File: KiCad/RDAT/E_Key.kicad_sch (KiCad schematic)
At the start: 0 parts

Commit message: Connected m.2 E Key
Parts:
- added C80, C81: 220nF/50V, A_HDJ_Library:C_0402_1005Metric, symbol Device:C_Small
- added C82, C84: 10uF/10V, A_HDJ_Library:C_0402_1005Metric, symbol Device:C
- added C83, C85: 100nF/50V, A_HDJ_Library:C_0402_1005Metric, symbol Device:C
- added H8: MountingHole_M2.0, A_HDJ_Library:MountingHole_2.75mm_M2_4.4mm_Pad_TopOnly, symbol Mechanical:MountingHole_Pad
- added J16: Bus_M.2_Socket_E, A_HDJ_Library:PCIe_M.2_Connectors_P=0.5mm_H=4.2mm_KeyE, symbol Connector:Bus_M.2_Socket_E
- added R72, R73: 0R/1%, A_HDJ_Library:R_0402_1005Metric, symbol Device:R
- added R74, R75: 10K/1%, A_HDJ_Library:R_0402_1005Metric, symbol Device:R
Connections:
- new net: J16.56 (~{W_DISABLE1}), R74.1
- new net: J16.50 (SUSCLK), R73.1
- new net: J16.54 (~{W_DISABLE2}), R75.2
- new net +3V3: C82.2, C83.2, C84.2, C85.2, J16.2 (3.3V), J16.4 (3.3V), J16.72 (3.3V), J16.74 (3.3V), R74.2, R75.1
- new net CON_PCIE_TX_0+: C80.2, J16.35 (PETp0)
- new net CON_PCIE_TX_0-: C81.2, J16.37 (PETn0)
- new net GND: C82.1, C83.1, C84.1, C85.1, H8.1, J16.1 (GND), J16.18 (GND), J16.33 (GND), J16.39 (GND), J16.45 (GND), J16.51 (GND), J16.57 (GND), J16.63 (GND), J16.69 (GND), J16.7 (GND), J16.75 (GND), J16.MP1, J16.MP2, R72.2
- new net PCIE_RX_0+: J16.41 (PERp0)
- new net PCIE_RX_0-: J16.43 (PERn0)
- new net PCIE_TX_0+: C80.1
- new net PCIE_TX_0-: C81.1
- new net REFCLKE+: J16.47 (REFCLKp0)
- new net REFCLKE-: J16.49 (REFCLKn0)
- new net SUSCLK: R73.2
- new net USB_2_P7+: J16.3 (USB_D+)
- new net USB_2_P7-: J16.5 (USB_D-)
- new net ~{CLKREQE}: J16.53 (~{CLKREQ0}), R72.1
- new net ~{PLT_RST}: J16.52 (~{PERST0})
- new net ~{WAKE}: J16.55 (~{PEWAKE0})
- no-connect marks 0 -> 38

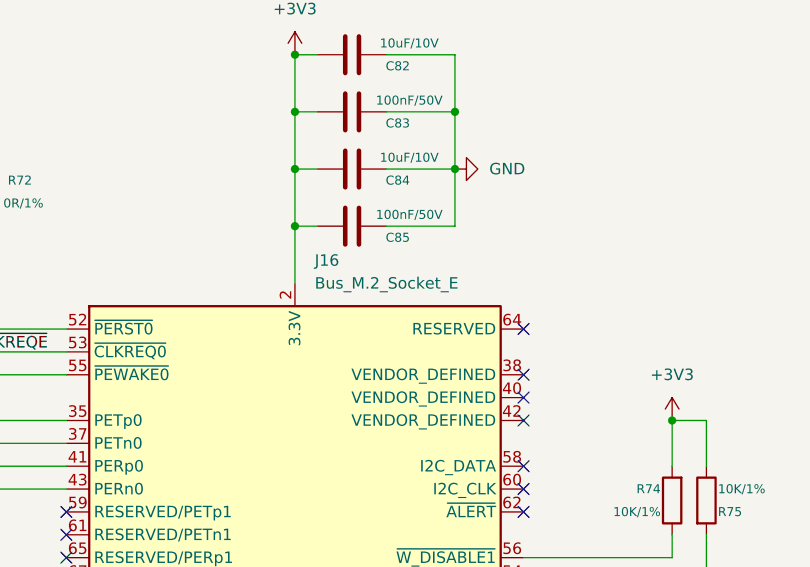
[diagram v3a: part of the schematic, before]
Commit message: Added Libs and DOCS
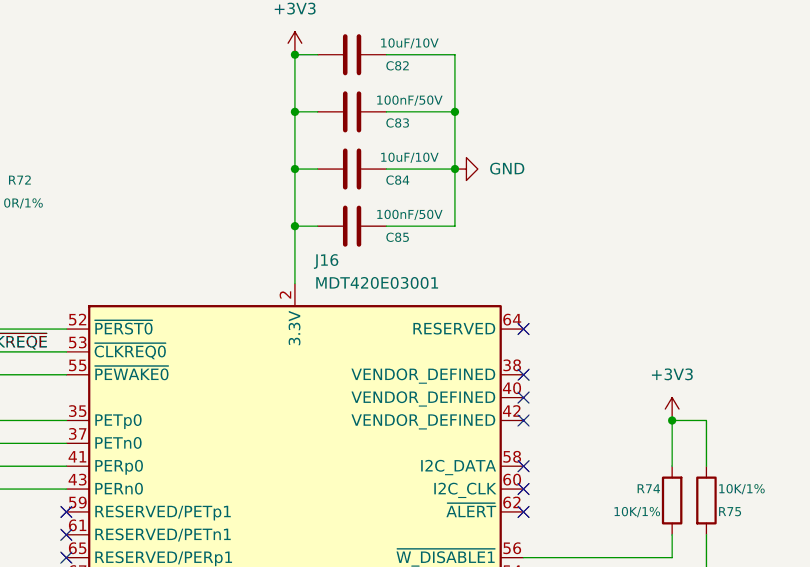
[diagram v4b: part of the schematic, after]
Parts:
- J16: value Bus_M.2_Socket_E -> MDT420E03001; footprint A_HDJ_Library:PCIe_M.2_Connectors_P=0.5mm_H=4.2mm_KeyE -> footprints:AMPHENOL_MDT420E03001; JLCPCB_LINK (none) -> https://jlcpcb.com/partdetail/AmphenolIcc-MDT420E03001/C599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
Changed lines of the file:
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@@
 			)
 		)
-		(property "Value" "Bus_M.2_Socket_E"
+		(property "Value" "MDT420E03001"
 			(at 139.3541 69.85 0)
 			(effects
@@
 			)
 		)
-		(property "Footprint" "A_HDJ_Library:PCIe_M.2_Connectors_P=0.5mm_H=4.2mm_KeyE"
+		(property "Footprint" "footprints:AMPHENOL_MDT420E03001"
 			(at 137.16 91.44 0)
 			(effects
@@
 			)
 		)
-		(property "Datasheet" "http://read.pudn.com/downloads794/doc/project/3133918/PCIe_M.2_Electromechanical_Spec_Rev1.0_Final_11012013_RS_Clean.pdf#page=150"
+		(property "Datasheet" "https://cdn.amphenol-cs.com/media/wysiwyg/files/documentation/datasheet/ssio/ssio_pcie_m2.pdf"
 			(at 137.16 91.44 0)
 			(effects
@@
 			)
 		)
-		(property "JLCPCB_LINK" ""
+		(property "JLCPCB_LINK" "https://jlcpcb.com/partdetail/AmphenolIcc-MDT420E03001/C599397"
 			(at 137.16 118.11 0)
 			(effects
@@
 					(size 1.27 1.27)
 				)
+				(hide yes)
 			)
 		)

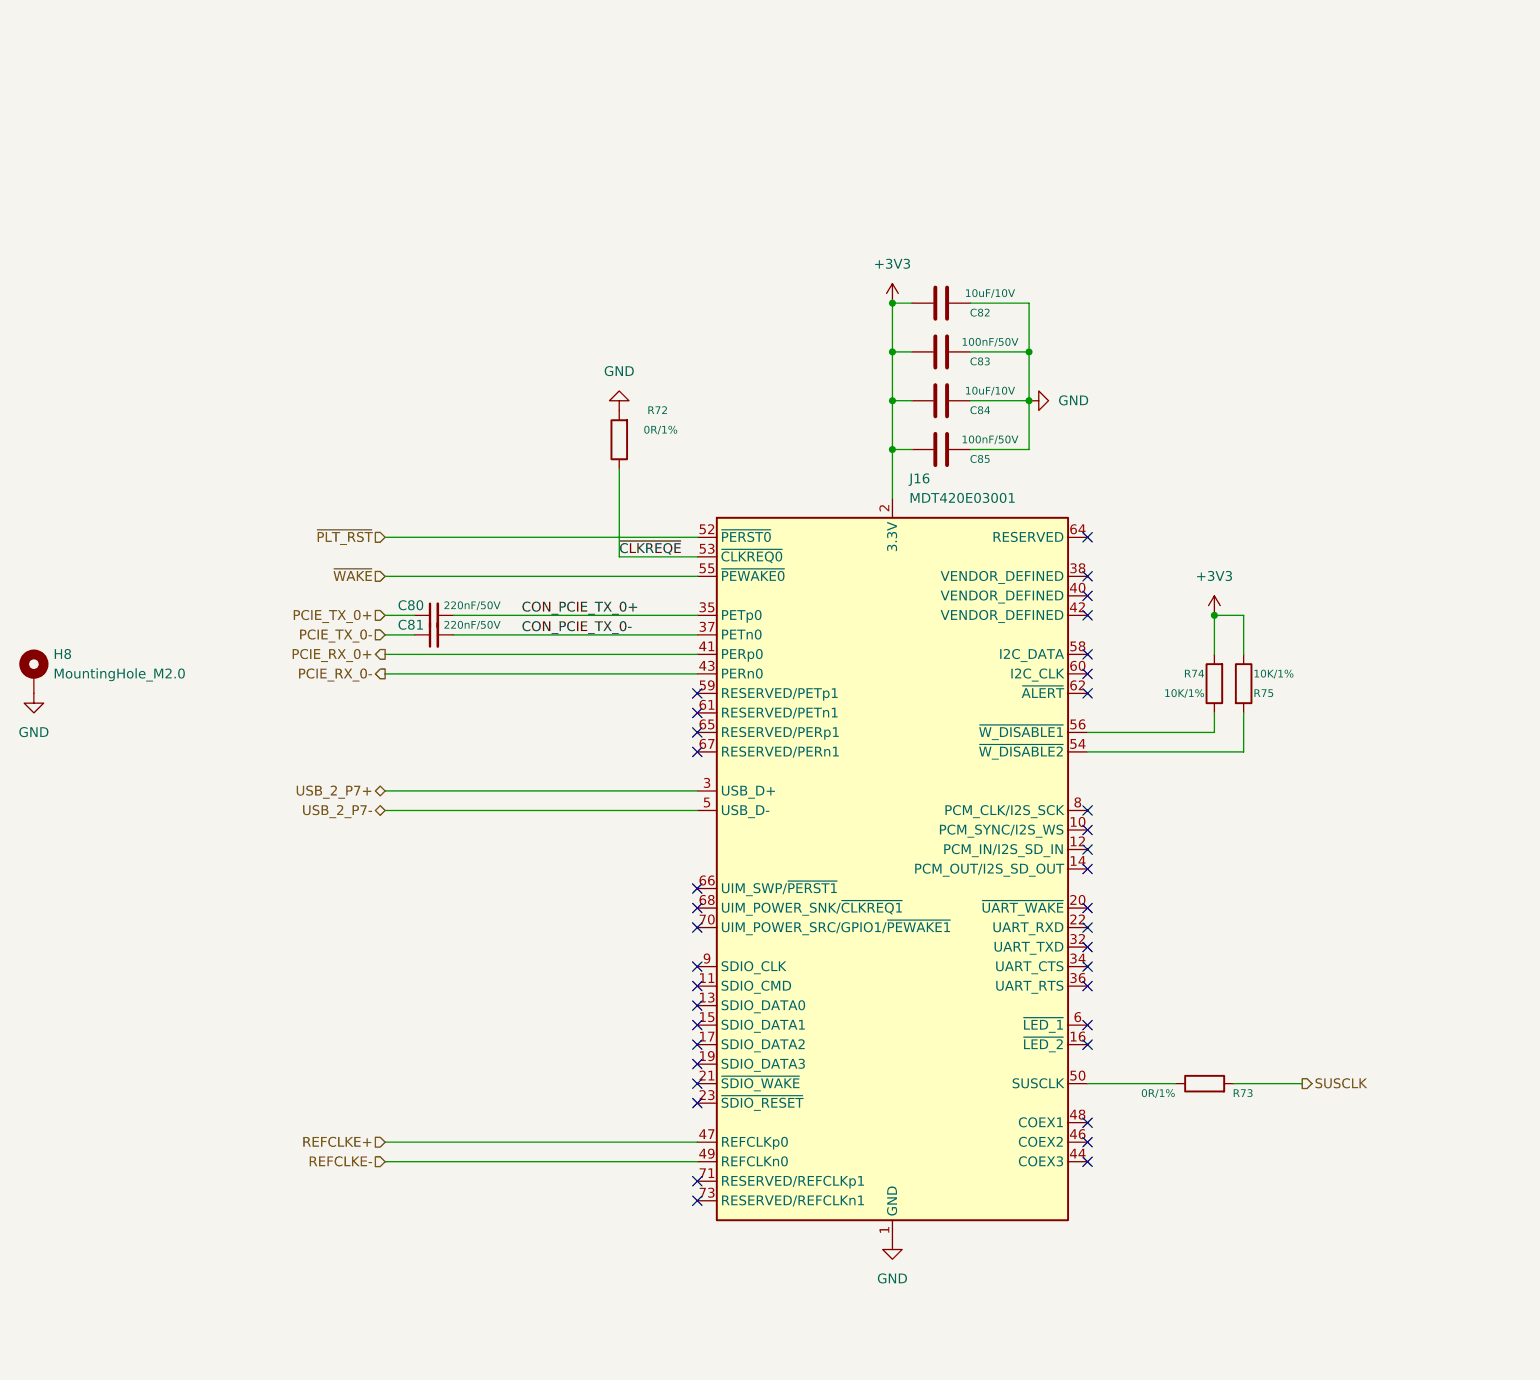
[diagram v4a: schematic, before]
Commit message: Sourced and documented all parts
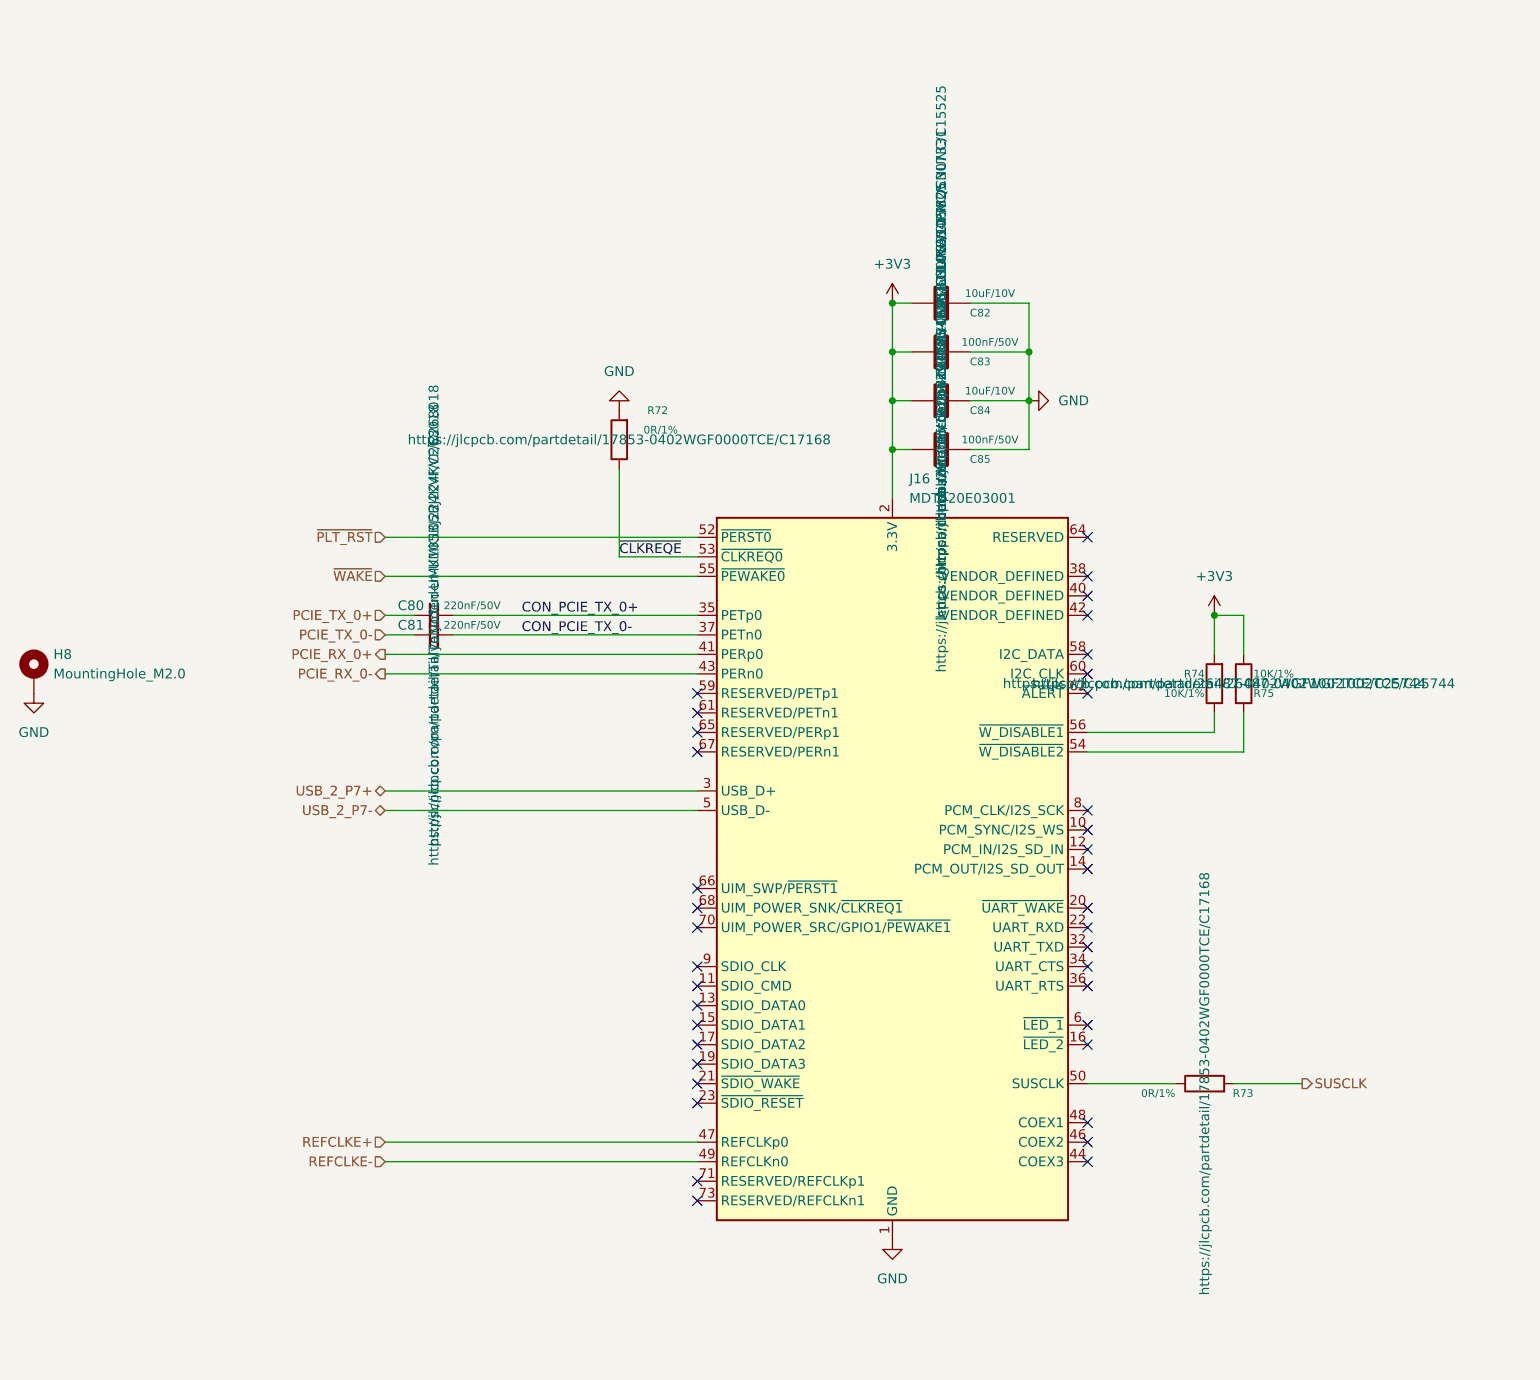
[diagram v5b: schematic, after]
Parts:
- C80, C81: JLCPCB_LINK (none) -> https://jlcpcb.com/partdetail/TaiyoYuden-UMK105BJ224KVF/C26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
- C82, C84: JLCPCB_LINK (none) -> https://jlcpcb.com/partdetail/16204-CL05A106MQ5NUNC/C15525
- C83, C85: JLCPCB_LINK (none) -> https://jlcpcb.com/partdetail/291005-CL05B104KB54PNC/C307331
- R72, R73: JLCPCB_LINK (none) -> https://jlcpcb.com/partdetail/17853-0402WGF0000TCE/C17168
- R74, R75: JLCPCB_LINK (none) -> https://jlcpcb.com/partdetail/26487-0402WGF1002TCE/C25744
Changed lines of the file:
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@@
 			)
 		)
-		(property "Datasheet" "~"
+		(property "Datasheet" "https://wmsc.lcsc.com/wmsc/upload/file/pdf/v2/lcsc/2108160930_Taiyo-Yuden-UMK105BJ224KV-F_C268018.pdf"
 			(at 77.47 85.09 0)
 			(effects
@@
 			)
 		)
-		(property "JLCPCB_LINK" ""
+		(property "JLCPCB_LINK" "https://jlcpcb.com/partdetail/TaiyoYuden-UMK105BJ224KVF/C268018"
 			(at 77.47 85.09 0)
 			(effects
@@
 			)
 		)
-		(property "Datasheet" "~"
+		(property "Datasheet" "https://wmsc.lcsc.com/wmsc/upload/file/pdf/v2/lcsc/2108160930_Taiyo-Yuden-UMK105BJ224KV-F_C268018.pdf"
 			(at 77.47 87.63 0)
 			(effects
@@
 			)
 		)
-		(property "JLCPCB_LINK" ""
+		(property "JLCPCB_LINK" "https://jlcpcb.com/partdetail/TaiyoYuden-UMK105BJ224KVF/C268018"
 			(at 77.47 87.63 0)
 			(effects
@@
 			)
 		)
-		(property "Datasheet" "~"
+		(property "Datasheet" "https://jlcpcb.com/api/file/downloadByFileSystemAccessId/8556212101498380288"
 			(at 179.07 93.98 0)
 			(effects
@@
 			)
 		)
-		(property "JLCPCB_LINK" ""
+		(property "JLCPCB_LINK" "https://jlcpcb.com/partdetail/26487-0402WGF1002TCE/C25744"
 			(at 179.07 93.98 0)
 			(effects
@@
 			)
 		)
-		(property "Datasheet" "~"
+		(property "Datasheet" "https://jlcpcb.com/api/file/downloadByFileSystemAccessId/8579707190011494400"
 			(at 143.51 57.15 0)
 			(effects
@@
 			)
 		)
-		(property "JLCPCB_LINK" ""
+		(property "JLCPCB_LINK" "https://jlcpcb.com/partdetail/16204-CL05A106MQ5NUNC/C15525"
 			(at 143.51 57.15 0)
 			(effects
@@
 			)
 		)
-		(property "Datasheet" "~"
+		(property "Datasheet" "https://jlcpcb.com/api/file/downloadByFileSystemAccessId/8579707190011494400"
 			(at 143.51 44.45 0)
 			(effects
@@
 			)
 		)
-		(property "JLCPCB_LINK" ""
+		(property "JLCPCB_LINK" "https://jlcpcb.com/partdetail/16204-CL05A106MQ5NUNC/C15525"
 			(at 143.51 44.45 0)
 			(effects
@@
 			)
 		)
-		(property "Datasheet" "~"
+		(property "Datasheet" "https://jlcpcb.com/api/file/downloadByFileSystemAccessId/8579705904671227904"
 			(at 177.8 146.05 0)
 			(effects
@@
 			)
 		)
-		(property "JLCPCB_LINK" ""
+		(property "JLCPCB_LINK" "https://jlcpcb.com/partdetail/17853-0402WGF0000TCE/C17168"
 			(at 177.8 146.05 0)
 			(effects
@@
 			)
 		)
-		(property "Datasheet" "~"
+		(property "Datasheet" "https://jlcpcb.com/api/file/downloadByFileSystemAccessId/8579705904671227904"
 			(at 101.6 62.23 0)
 			(effects
@@
 			)
 		)
-		(property "JLCPCB_LINK" ""
+		(property "JLCPCB_LINK" "https://jlcpcb.com/partdetail/17853-0402WGF0000TCE/C17168"
 			(at 101.6 62.23 0)
 			(effects
@@
 			)
 		)
-		(property "Datasheet" "~"
+		(property "Datasheet" "https://jlcpcb.com/api/file/downloadByFileSystemAccessId/8554627388281098240"
 			(at 143.51 63.5 0)
 			(effects
@@
 			)
 		)
-		(property "JLCPCB_LINK" ""
+		(property "JLCPCB_LINK" "https://jlcpcb.com/partdetail/291005-CL05B104KB54PNC/C307331"
 			(at 143.51 63.5 0)
 			(effects
@@
 			)
 		)
-		(property "Datasheet" "~"
+		(property "Datasheet" "https://jlcpcb.com/api/file/downloadByFileSystemAccessId/8554627388281098240"
 			(at 143.51 50.8 0)
 			(effects
@@
 			)
 		)
-		(property "JLCPCB_LINK" ""
+		(property "JLCPCB_LINK" "https://jlcpcb.com/partdetail/291005-CL05B104KB54PNC/C307331"
 			(at 143.51 50.8 0)
 			(effects
@@
 			)
 		)
-		(property "Datasheet" "~"
+		(property "Datasheet" "https://jlcpcb.com/api/file/downloadByFileSystemAccessId/8556212101498380288"
 			(at 182.88 93.98 0)
 			(effects
@@
 			)
 		)
-		(property "JLCPCB_LINK" ""
+		(property "JLCPCB_LINK" "https://jlcpcb.com/partdetail/26487-0402WGF1002TCE/C25744"
 			(at 182.88 93.98 0)
 			(effects

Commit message: Push before Board Layout
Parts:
- C80, C81, C82, C83, C84, C85: footprint A_HDJ_Library:C_0402_1005Metric -> Capacitor_SMD:C_0402_1005Metric
- H8: footprint A_HDJ_Library:MountingHole_2.75mm_M2_4.4mm_Pad_TopOnly -> MountingHole:MountingHole_2.2mm_M2_Pad_TopBottom
- R72, R73, R74, R75: footprint A_HDJ_Library:R_0402_1005Metric -> Resistor_SMD:R_0402_1005Metric
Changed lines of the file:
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@@
 			)
 		)
-		(property "Footprint" "A_HDJ_Library:C_0402_1005Metric"
+		(property "Footprint" "Capacitor_SMD:C_0402_1005Metric"
 			(at 77.47 85.09 0)
 			(effects
@@
 					(size 1.27 1.27)
 				)
+				(hide yes)
 			)
 		)
@@
 			)
 		)
-		(property "Footprint" "A_HDJ_Library:C_0402_1005Metric"
+		(property "Footprint" "Capacitor_SMD:C_0402_1005Metric"
 			(at 77.47 87.63 0)
 			(effects
@@
 					(size 1.27 1.27)
 				)
+				(hide yes)
 			)
 		)
@@
 			)
 		)
-		(property "Footprint" "A_HDJ_Library:R_0402_1005Metric"
+		(property "Footprint" "Resistor_SMD:R_0402_1005Metric"
 			(at 180.848 93.98 90)
 			(effects
@@
 			)
 		)
-		(property "Footprint" "A_HDJ_Library:C_0402_1005Metric"
+		(property "Footprint" "Capacitor_SMD:C_0402_1005Metric"
 			(at 139.7 58.1152 0)
 			(effects
@@
 					(size 1.27 1.27)
 				)
+				(hide yes)
 			)
 		)
@@
 			)
 		)
-		(property "Footprint" "A_HDJ_Library:C_0402_1005Metric"
+		(property "Footprint" "Capacitor_SMD:C_0402_1005Metric"
 			(at 139.7 45.4152 0)
 			(effects
@@
 					(size 1.27 1.27)
 				)
+				(hide yes)
 			)
 		)
@@
 			)
 		)
-		(property "Footprint" "A_HDJ_Library:R_0402_1005Metric"
+		(property "Footprint" "Resistor_SMD:R_0402_1005Metric"
 			(at 177.8 147.828 90)
 			(effects
@@
 			)
 		)
-		(property "Footprint" "A_HDJ_Library:R_0402_1005Metric"
+		(property "Footprint" "Resistor_SMD:R_0402_1005Metric"
 			(at 103.378 62.23 90)
 			(effects
@@
 			)
 		)
-		(property "Footprint" "A_HDJ_Library:MountingHole_2.75mm_M2_4.4mm_Pad_TopOnly"
+		(property "Footprint" "MountingHole:MountingHole_2.2mm_M2_Pad_TopBottom"
 			(at 25.4 92.71 0)
 			(effects
@@
 			)
 		)
-		(property "Footprint" "A_HDJ_Library:C_0402_1005Metric"
+		(property "Footprint" "Capacitor_SMD:C_0402_1005Metric"
 			(at 139.7 64.4652 0)
 			(effects
@@
 					(size 1.27 1.27)
 				)
+				(hide yes)
 			)
 		)
@@
 			)
 		)
-		(property "Footprint" "A_HDJ_Library:C_0402_1005Metric"
+		(property "Footprint" "Capacitor_SMD:C_0402_1005Metric"
 			(at 139.7 51.7652 0)
 			(effects
@@
 					(size 1.27 1.27)
 				)
+				(hide yes)
 			)
 		)
@@
 			)
 		)
-		(property "Footprint" "A_HDJ_Library:R_0402_1005Metric"
+		(property "Footprint" "Resistor_SMD:R_0402_1005Metric"
 			(at 181.102 93.98 90)
 			(effects

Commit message: Placed a lot of components
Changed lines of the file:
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@@
 					(size 1.27 1.27)
 				)
+				(hide yes)
 			)
 		)
@@
 					(size 1.27 1.27)
 				)
+				(hide yes)
 			)
 		)
@@
 					(size 1.27 1.27)
 				)
+				(hide yes)
 			)
 		)
@@
 					(size 1.27 1.27)
 				)
-			)
-		)
+				(hide yes)
+			)
+		)

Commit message: End Of day commit
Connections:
- net GND: now also J16.S1 (Sheild), J16.S2 (Sheild); no longer J16.MP1, J16.MP2
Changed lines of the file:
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@@
+	(wire
+		(pts
+			(xy 137.16 166.37) (xy 137.16 171.45)
+		)
+		(stroke
+			(width 0)
+			(type default)
+		)
+	)
 	(wire
 		(pts
@@
 		(pin "75"
 		)
-		(pin "MP1"
-		)
-		(pin "MP2"
+		(pin "S1"
+		)
+		(pin "S2"
 		)
 		(instances
@@
 	(symbol
 		(lib_id "power:GND")
-		(at 137.16 166.37 0)
+		(at 137.16 171.45 0)
 		(unit 1)
 		(exclude_from_sim no)
@@
 		(fields_autoplaced yes)
 		(property "Reference" "#PWR087"
-			(at 137.16 172.72 0)
+			(at 137.16 177.8 0)
 			(effects
 				(font
@@
 		)
 		(property "Value" "GND"
+			(at 137.16 176.53 0)
+			(effects
+				(font
+					(size 1.27 1.27)
+				)
+			)
+		)
+		(property "Footprint" ""
 			(at 137.16 171.45 0)
 			(effects
@@
 					(size 1.27 1.27)
 				)
-			)
-		)
-		(property "Footprint" ""
-			(at 137.16 166.37 0)
-			(effects
-				(font
-					(size 1.27 1.27)
-				)
 				(hide yes)
 			)
 		)
 		(property "Datasheet" ""
-			(at 137.16 166.37 0)
+			(at 137.16 171.45 0)
 			(effects
 				(font
@@
 		)
 		(property "Description" ""
-			(at 137.16 166.37 0)
-			(effects
-				(font
+			(at 137.16 171.45 0)
+			(effects
+				(font
